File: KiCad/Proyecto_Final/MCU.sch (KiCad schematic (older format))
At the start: 112 parts, among them J10 PF, J11 PB, J12 PE, J13 PA, J14 PD, J15 SPI4, J16 OutEn, J17 CFG_SEL, J18 CTRL_MODE, J3 5v, J4 I2C1, J5 ARM SWD, J6 USB_B_Micro, J7 Boot_Select, J8 PG, J9 PC, SW1 Reset, U11 TLV1117-33, U12 USBLC6-2SC6, U13 STM32F723ZCTx, U14 5P49V5929, Y1 25MHz

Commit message: Avance PCB.
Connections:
- net B1: now also U13.123 (PD7); no longer U13.129 (PG14)
- net B2: now also U13.124 (PG9); no longer U13.128 (PG13)
- net B3: now also U13.125 (PG10); no longer U13.127 (PG12)
- net B5: now also U13.127 (PG12); no longer U13.125 (PG10)
- net B6: now also U13.129 (PG14); no longer U13.124 (PG9)
- net B7: now also U13.128 (PG13); no longer U13.123 (PD7)
- net Filt_Bypass: now also U13.69 (PB10); no longer U13.14 (PF4)
- net Filtro: now also U13.70 (PB11); no longer U13.15 (PF5)
- net PB10: no longer U13.69 (PB10)
- net PB11: no longer U13.70 (PB11)
- net PE11: no longer U13.64 (PE11)
- net PE12: no longer U13.65 (PE12)
- net PE13: no longer U13.66 (PE13)
- net PE14: no longer U13.67 (PE14)
- net PE15: no longer U13.68 (PE15)
- net Rx_Amp: now also U13.67 (PE14); no longer U13.13 (PF3)
- net Rx_Amp_Bypass: now also U13.66 (PE13); no longer U13.12 (PF2)
- net Rx_Amp_Pwr: now also U13.68 (PE15); no longer U13.11 (PF1)
- net Rx_Mix: now also U13.65 (PE12); no longer U13.10 (PF0)
- net Rx_Mix_Bypass: now also U13.64 (PE11); no longer U13.7 (PC13)
- net SPI1_CS0: now also U13.37 (PA3); no longer U13.44 (PC4)
- net Trx_Enable: now also U13.47 (PB1); no longer U13.46 (PB0)
- net Trx_Rx_Enable: now also U13.46 (PB0); no longer U13.47 (PB1)
- net PA3 renamed PC4
- net PC4: now also U13.44 (PC4); no longer U13.37 (PA3)
- new net PC13: U13.7 (PC13)
- new net PF0: U13.10 (PF0)
- new net PF1: U13.11 (PF1)
- new net PF2: U13.12 (PF2)
- new net PF3: U13.13 (PF3)
- new net PF4: U13.14 (PF4)
- new net PF5: U13.15 (PF5)
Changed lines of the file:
@@
 Text GLabel 10450 3350 2    50   Input ~ 0
 SPI1_MOSI
-Text GLabel 10450 6450 2    50   Input ~ 0
+Text GLabel 10450 2950 2    50   Input ~ 0
 SPI1_CS0
 Text GLabel 10450 6550 2    50   Input ~ 0
@@
 Text GLabel 10450 5050 2    50   Input ~ 0
 I2C1_SDA
-Text GLabel 7850 6550 0    50   Input ~ 0
+Text GLabel 10450 5450 2    50   Input ~ 0
 Filtro
-Text GLabel 7850 6450 0    50   Input ~ 0
+Text GLabel 10450 5350 2    50   Input ~ 0
 Filt_Bypass
-Text GLabel 7850 6350 0    50   Input ~ 0
+Text GLabel 7850 9150 0    50   Input ~ 0
 Rx_Amp
-Text GLabel 7850 6250 0    50   Input ~ 0
+Text GLabel 7850 9050 0    50   Input ~ 0
 Rx_Amp_Bypass
-Text GLabel 7850 6150 0    50   Input ~ 0
+Text GLabel 7850 9250 0    50   Input ~ 0
 Rx_Amp_Pwr
-Text GLabel 7850 6050 0    50   Input ~ 0
+Text GLabel 7850 8950 0    50   Input ~ 0
 Rx_Mix
-Text GLabel 10450 7350 2    50   Input ~ 0
+Text GLabel 7850 8850 0    50   Input ~ 0
 Rx_Mix_Bypass
 $Comp
@@
 	5800 3900 5900 3900
 Connection ~ 5900 3900
+Text GLabel 10450 4450 2    50   Input ~ 0
+Trx_Enable
 Text GLabel 10450 4350 2    50   Input ~ 0
-Trx_Enable
-Text GLabel 10450 4450 2    50   Input ~ 0
 Trx_Rx_Enable
 Text GLabel 10450 6250 2    50   Input ~ 0
@@
 Text GLabel 7850 7750 0    50   Input ~ 0
 RXHP
-Text GLabel 7850 5750 0    50   Input ~ 0
+Text GLabel 10450 8450 2    50   Input ~ 0
 B1
-Text GLabel 7850 5650 0    50   Input ~ 0
+Text GLabel 7850 5250 0    50   Input ~ 0
 B2
-Text GLabel 7850 5550 0    50   Input ~ 0
+Text GLabel 7850 5350 0    50   Input ~ 0
 B3
 Text GLabel 7850 5450 0    50   Input ~ 0
 B4
-Text GLabel 7850 5350 0    50   Input ~ 0
+Text GLabel 7850 5550 0    50   Input ~ 0
 B5
-Text GLabel 7850 5250 0    50   Input ~ 0
+Text GLabel 7850 5750 0    50   Input ~ 0
 B6
-Text GLabel 10450 8450 2    50   Input ~ 0
+Text GLabel 7850 5650 0    50   Input ~ 0
 B7
 $Comp
@@
 Text GLabel 7850 8750 0    50   Input ~ 0
 PE10
-Text GLabel 7850 8850 0    50   Input ~ 0
-PE11
-Text GLabel 7850 8950 0    50   Input ~ 0
-PE12
-Text GLabel 7850 9050 0    50   Input ~ 0
-PE13
-Text GLabel 7850 9150 0    50   Input ~ 0
-PE14
-Text GLabel 7850 9250 0    50   Input ~ 0
-PE15
+Text GLabel 10450 7350 2    50   Input ~ 0
+PC13
+Text GLabel 7850 6050 0    50   Input ~ 0
+PF0
+Text GLabel 7850 6250 0    50   Input ~ 0
+PF2
+Text GLabel 7850 6350 0    50   Input ~ 0
+PF3
+Text GLabel 7850 6150 0    50   Input ~ 0
+PF1
 Text GLabel 12950 6850 0    50   Input ~ 0
 PE1
@@
 Text GLabel 10450 5250 2    50   Input ~ 0
 PB9
-Text GLabel 10450 5350 2    50   Input ~ 0
-PB10
-Text GLabel 10450 5450 2    50   Input ~ 0
-PB11
+Text GLabel 7850 6450 0    50   Input ~ 0
+PF4
+Text GLabel 7850 6550 0    50   Input ~ 0
+PF5
 Text GLabel 10450 5550 2    50   Input ~ 0
 PB12
@@
 Text GLabel 10450 3050 2    50   Input ~ 0
 PA4
-Text GLabel 10450 2950 2    50   Input ~ 0
-PA3
+Text GLabel 10450 6450 2    50   Input ~ 0
+PC4
 Text GLabel 10450 2850 2    50   Input ~ 0
 PA2
@@
 Text GLabel 14350 7750 0    50   Input ~ 0
 PA4
-Text GLabel 14350 7650 0    50   Input ~ 0
-PA3
 Text GLabel 14350 7550 0    50   Input ~ 0
 PA2
@@
 	1    0    0    -1
 $EndComp
+Text GLabel 14350 7650 0    50   Input ~ 0
+PC4
 $EndSCHEMATC

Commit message: Sección RF terminada.
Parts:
- renumbered J11 to J10, J12 to J11, J13 to J12, J14 to J13, J15 to J14, J16 to J15, J17 to J16, J18 to J17, J3 to J2, J4 to J3, J5 to J4, J6 to J5, J7 to J6, J8 to J7, J9 to J8, J10 to J9, R17 to R15, R18 to R16, R19 to R17, R20 to R18, R21 to R19, R22 to R20, R23 to R21, R24 to R22, R25 to R23, R26 to R24, R27 to R25, R28 to R26, R29 to R27, R30 to R28, R31 to R29
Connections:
- net ADC_22MHz is gone; now on net MCU_CLK: R21.2, TP31.1
- net MCU_CLK: no longer R28.2, R29.2, TP35.1
- net MIX_CLK: now also R25.2, TP34.1; no longer R23.2, TP33.1
- net Trx_CLK: now also R23.2, TP33.1; no longer R25.2, TP34.1
- net ADC_45MHz renamed CLK_ADC
- new net Clk_Out0: R28.2, R29.2, TP35.1

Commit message: Avances PCB.
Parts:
- removed J16: CFG_SEL, Connector_PinHeader_2.54mm:PinHeader_2x04_P2.54mm_Vertical_SMD, symbol Connector_Generic:Conn_02x04_Counter_Clockwise
- removed J17: CTRL_MODE, Connector_PinHeader_2.54mm:PinHeader_2x01_P2.54mm_Vertical_SMD, symbol Connector_Generic:Conn_02x01
- removed R26, R27, R28: 10k, Resistor_SMD:R_0402_1005Metric, symbol Device:R
- added H1, H2, H3, H4: MountingHole, MountingHole:MountingHole_3.2mm_M3_Pad_Via, symbol Mechanical:MountingHole
- added J16: CLK_OUT0, Tesis2020-21:RFSOLUTIONS_CON-SMA-EDGE-S, symbol Connector:Conn_Coaxial
- added JP1: SolderJumper, Jumper:SolderJumper-2_P1.3mm_Open_RoundedPad1.0x1.5mm, symbol Jumper:SolderJumper_2_Open
- R17, R18: value 10k -> 4.7k
- renumbered R29 to R26
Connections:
- net GND: now also J16.2 (Ext)
- net USB_CONN_D+: now also U12.3 (I/O2); no longer U12.1 (I/O1)
- net USB_CONN_D-: now also U12.1 (I/O1); no longer U12.3 (I/O2)
- net USB_D+: now also U12.4 (I/O2); no longer U12.6 (I/O1)
- net USB_D-: now also U12.6 (I/O1); no longer U12.4 (I/O2)
- net at U14.24 (OUT0_SEL_I2CB): now also JP1.1 (A); no longer R26.1
- net Clk_Out0: no longer names the net of R26.2, TP35.1
- net Clk_Out0: now also J16.1 (In)
- new net: JP1.2 (B), R26.1
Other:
- note removed: "0 = I2C\n1 = HW"
- note removed: "00 = Config0\n01 = Config1\n10 = Config2\n11 = Config3"
- moved on the sheet: C109, C110, R26, TP35, TP36, TP37, TP38, TP39, TP40, TP41, TP42, TP43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

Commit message: Avances PCB.
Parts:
- removed H1, H2, H3, H4: MountingHole, MountingHole:MountingHole_3.2mm_M3_Pad_Via, symbol Mechanical:MountingHole
- removed J15: OutEn, Connector_PinHeader_2.54mm:PinHeader_2x02_P2.54mm_Vertical_SMD, symbol Connector_Generic:Conn_02x02_Odd_Even
- removed J2: 5v, Connector_PinHeader_2.54mm:PinHeader_2x01_P2.54mm_Vertical_SMD, symbol Connector_Generic:Conn_01x02
- removed J6: Boot_Select, Connector_PinHeader_2.54mm:PinHeader_2x02_P2.54mm_Vertical_SMD, symbol Connector_Generic:Conn_02x02_Odd_Even
- removed U11: TLV1117-33, Package_TO_SOT_SMD:SOT-223-3_TabPin2, symbol Regulator_Linear:TLV1117-33
- added H1, H2, H3, H4: MountingHole_Pad, MountingHole:MountingHole_3.2mm_M3_Pad_Via, symbol Mechanical:MountingHole_Pad
- added J14: OutEn, Connector_PinHeader_2.54mm:PinHeader_1x03_P2.54mm_Vertical, symbol Connector_Generic:Conn_01x03
- added J5: Boot_Select, Connector_PinHeader_2.54mm:PinHeader_1x03_P2.54mm_Vertical, symbol Connector_Generic:Conn_01x03
- added U11: AMS1117-3.3, Package_TO_SOT_SMD:SOT-223-3_TabPin2, symbol Regulator_Linear:AMS1117-3.3
- renumbered J11 to J10, J12 to J11, J13 to J12, J14 to J13, J16 to J15, J3 to J2, J4 to J3, J5 to J4, J7 to J6, J8 to J7, J9 to J8, J10 to J9
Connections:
- net +3V3: now also J14.1 (Pin_1), J5.1 (Pin_1), U11.2 (VO)
- net GND: now also H1.1, H2.1, H3.1, H4.1, J14.3 (Pin_3), J5.3 (Pin_3), U11.1 (GND)
- net PE10: no longer U13.63 (PE10)
- net at C90.1, D1.1 (K), FB1.1: now also U11.3 (VI)
- net at R20.1: now also J5.2 (Pin_2)
- net at R24.1: now also J14.2 (Pin_2)
- new net RESETX: U13.63 (PE10)
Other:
- moved on the sheet: R19, R20, R24

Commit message: Avances PCB.
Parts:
- removed TP21, TP22, TP23, TP24: TestPoint, TestPoint:TestPoint_Pad_D1.0mm, symbol Connector:TestPoint
- renumbered C75 to C28, C76 to C29, C77 to C30, C78 to C31, C79 to C32, C80 to C33, C81 to C34, C82 to C35, C83 to C36, C84 to C37, C85 to C38, C86 to C39, C87 to C40, C88 to C41, C89 to C42, C90 to C43, C91 to C44, C92 to C45, C93 to C46, C94 to C47, C95 to C48, C96 to C49, C97 to C50, C98 to C51, C99 to C52, C100 to C53, C101 to C54, C102 to C55, C103 to C56, C104 to C57, C105 to C58, C106 to C59, C107 to C60, C108 to C61, C109 to C62, C110 to C63, J2 to J1, J11 to J10, J12 to J11, J13 to J12, J14 to J13, J15 to J14, J3 to J2, J4 to J3, J5 to J4, J6 to J5, J7 to J6, J8 to J7, J9 to J8, J10 to J9, R16 to R10, R17 to R11, R18 to R12, R19 to R13, R20 to R14, R21 to R15, R22 to R16, R23 to R17, R24 to R18, R25 to R19, R26 to R20, R15 to R9, TP25 to TP21, TP26 to TP22, TP27 to TP23, TP28 to TP24, TP29 to TP25, TP30 to TP26, TP31 to TP27, TP32 to TP28, TP33 to TP29, TP34 to TP30, TP35 to TP31, TP36 to TP32, TP37 to TP33, TP38 to TP34, TP39 to TP35, TP40 to TP36, TP41 to TP37, TP42 to TP38, TP43 to TP39, TP44 to TP40, TP45 to TP41, U11 to U3, U12 to U4, U13 to U5, U14 to U6

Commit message: Eliminadas conexiones innecesarias del transceptor.
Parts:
- J2: footprint Connector_PinHeader_1.27mm:PinHeader_2x05_P1.27mm_Vertical_SMD -> Connector_PinHeader_2.54mm:PinHeader_2x05_P2.54mm_Vertical_SMD
- renumbered R9 to R10, R10 to R11, R11 to R12, R12 to R13, R13 to R14, R14 to R15, R15 to R16, R16 to R17, R17 to R18, R18 to R19, R19 to R20, R20 to R21

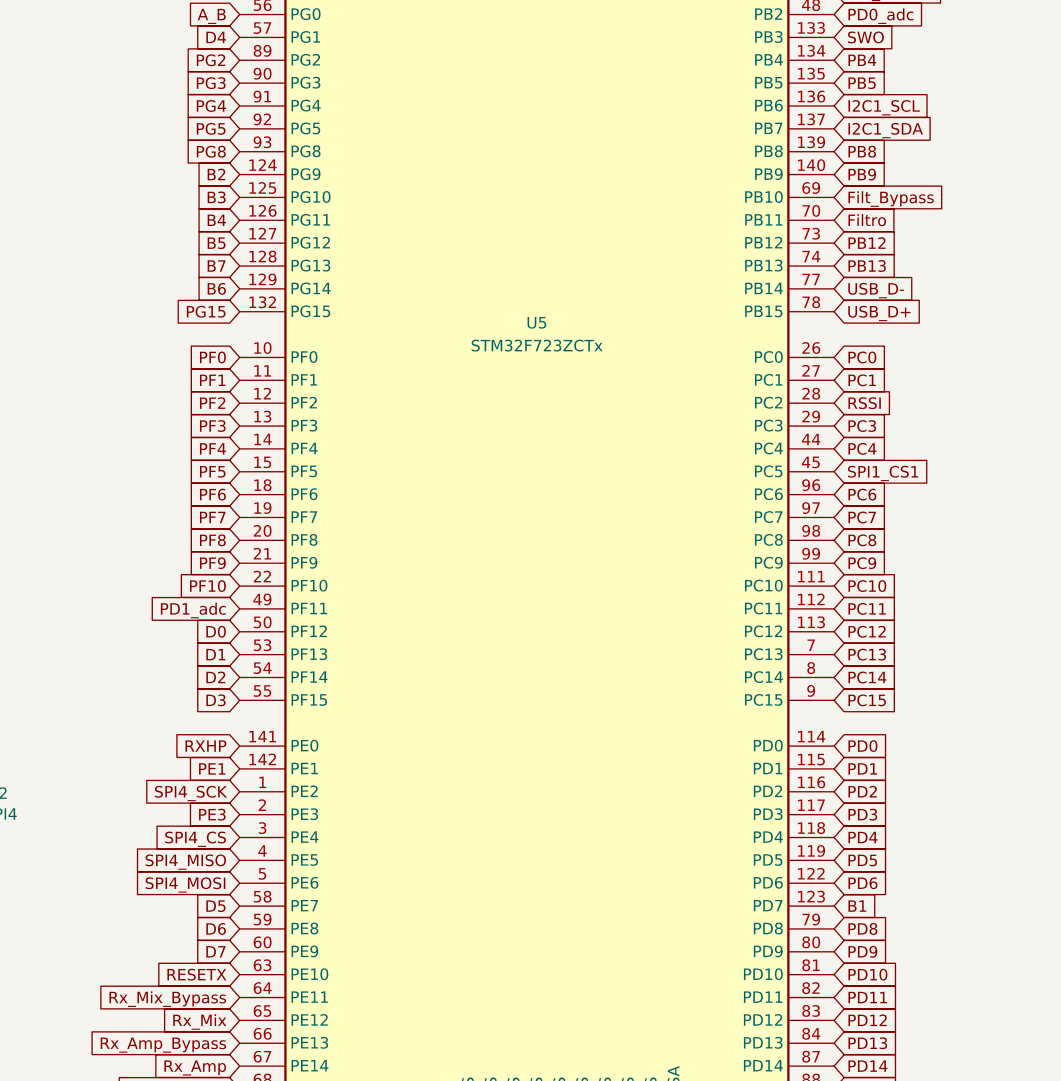
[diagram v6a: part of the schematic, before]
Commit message: Pistas reacomodadas para mejor ruteo.
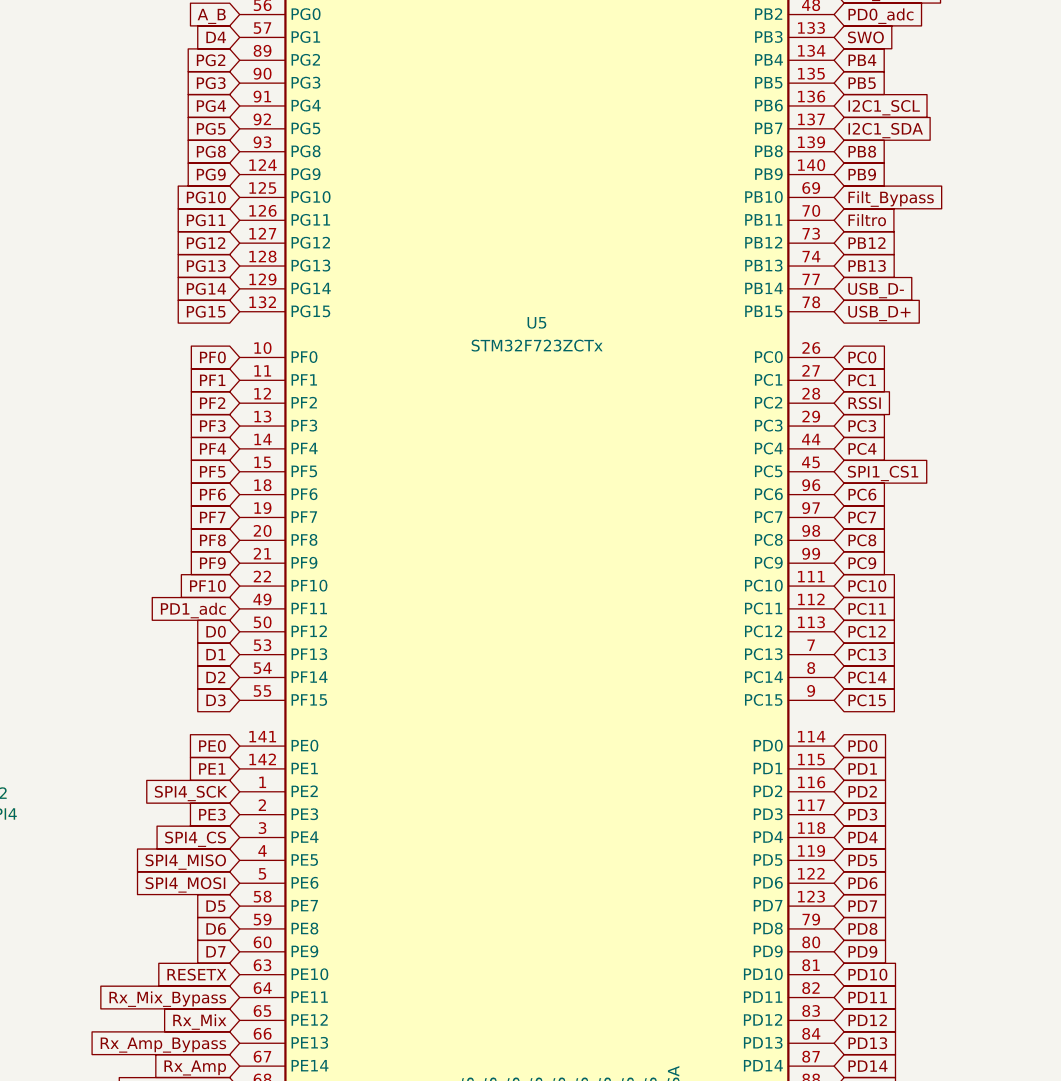
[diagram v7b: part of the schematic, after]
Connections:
- net RXHP: no longer U5.141 (PE0)
- net B1 renamed PD7
- net B2 renamed PG9
- net B3 renamed PG10
- net B4 renamed PG11
- net B5 renamed PG12
- net B6 renamed PG14
- net B7 renamed PG13
- new net PE0: U5.141 (PE0)
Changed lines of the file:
@@
 RSSI
 Text GLabel 7850 7750 0    50   Input ~ 0
-RXHP
+PE0
 Text GLabel 10450 8450 2    50   Input ~ 0
-B1
+PD7
 Text GLabel 7850 5250 0    50   Input ~ 0
-B2
+PG9
 Text GLabel 7850 5350 0    50   Input ~ 0
-B3
+PG10
 Text GLabel 7850 5450 0    50   Input ~ 0
-B4
+PG11
 Text GLabel 7850 5550 0    50   Input ~ 0
-B5
+PG12
 Text GLabel 7850 5750 0    50   Input ~ 0
-B6
+PG14
 Text GLabel 7850 5650 0    50   Input ~ 0
-B7
+PG13
 $Comp
 L Device:C C45

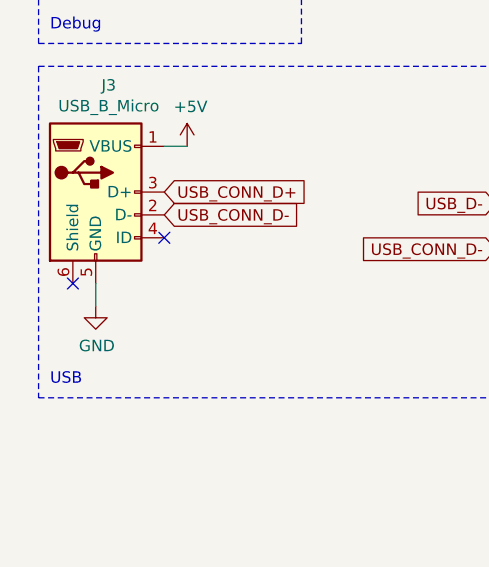
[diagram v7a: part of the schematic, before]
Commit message: Avances PCBv2.
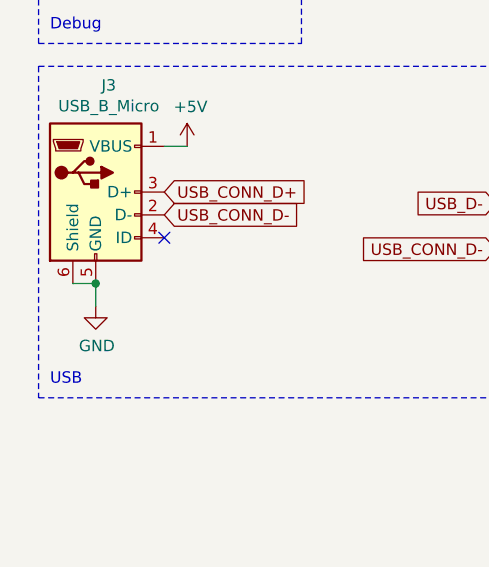
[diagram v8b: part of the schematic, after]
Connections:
- net GND: now also J3.6 (Shield)
- no-connect marks 15 -> 14
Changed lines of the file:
@@
 	1    0    0    -1
 $EndComp
-NoConn ~ 850  5550
 NoConn ~ 1250 5350
 Text GLabel 3500 5200 2    50   Input ~ 0
@@
 Wire Wire Line
 	2450 9400 2650 9400
+Wire Wire Line
+	850  5550 950  5550
+Connection ~ 950  5550
 $EndSCHEMATC
